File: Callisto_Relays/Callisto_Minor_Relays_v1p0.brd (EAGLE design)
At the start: 75 x 100 mm, 34 parts, among them J1 2-pos, J10 RJ45_TH_VERT, J2 RJ45_TH_VERT, J5 2-pos, J6 RJ45_TH_VERT, J7 2-pos, J8 RJ45_TH_VERT, J9 2-pos, U2 NPN, U3 NPN, U4 NPN, U5 NPN

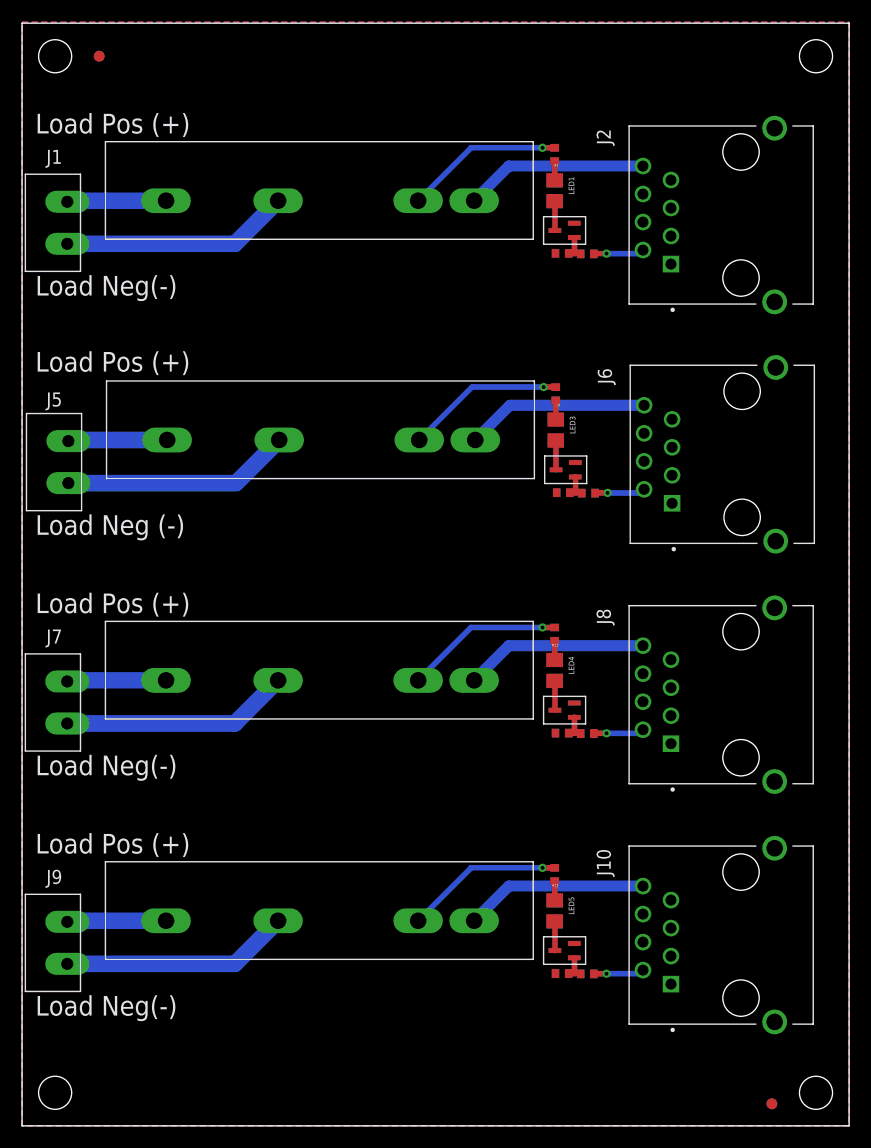
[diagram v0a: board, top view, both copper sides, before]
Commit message: Updated relay board.
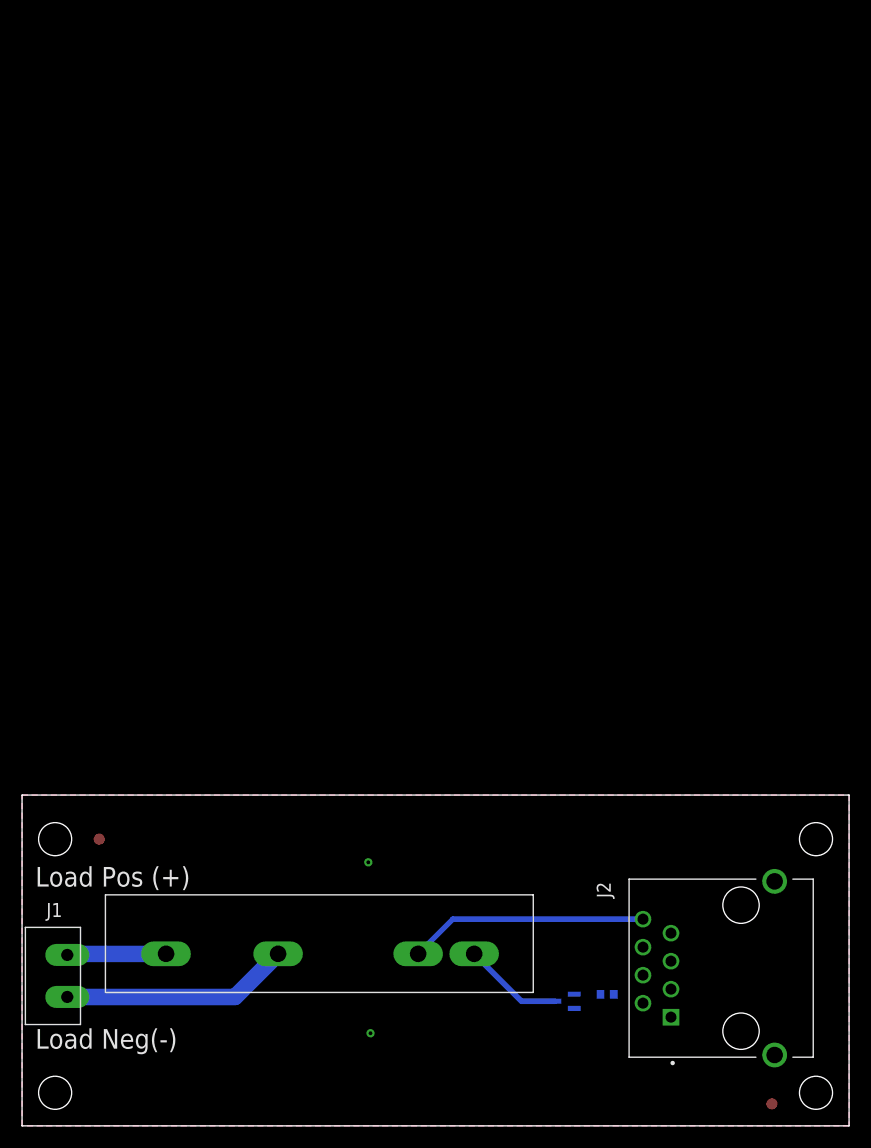
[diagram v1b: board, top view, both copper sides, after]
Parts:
- removed J10, J6, J8: RJ45_TH_VERT, 3D_MIG_Controller:ASSMANN_A-2014-2S-4-N-R
- removed J5, J7, J9: 2-pos, 3D_MIG_Controller:2_3.81MM_PITCH
- removed LED1, LED3, LED4, LED5: Green, 3D_MIG_Controller:0805
- removed R10, R13, R7: 1K, 3D_MIG_Controller:0402
- removed R11, R14, R2, R8: 10K, 3D_MIG_Controller:0402
- removed R12, R15, R3, R9: 470R0, 3D_MIG_Controller:0402
- removed U$5, U$6, U$7: RELAY_KYOTO_KF0604D, 3D_MIG_Controller:RELAY_KYOTO_KF0604D
- removed U3, U4, U5: NPN, 3D_MIG_Controller:SOT323
- R1: value 1K -> 500R0
- moved U$1 71.0 mm to (7.00, 26.0)
- moved U2 69.9 mm to (49.2, 11.3), flipped to the bottom, turned to 270 degrees
- moved U$3 68.3 mm to (41.0, 15.6)
- moved J1 68.3 mm to (4.10, 15.5)
- moved J2 68.3 mm to (65.2, 14.3)
- moved R1 67.2 mm to (53.1, 11.9), flipped to the bottom, turned to 90 degrees
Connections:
- removed net N$1: LED1.1, R3.P$1
- removed net N$10: LED4.1, R12.P$1
- removed net N$11: LED4.2, U4.3
- removed net N$12: R12.P$2, U$6.P$2
- removed net N$13: R7.P$2, R8.P$1, U3.1
- removed net N$14: LED3.1, R9.P$1
- removed net N$15: LED3.2, U3.3
- removed net N$16: R9.P$2, U$5.P$2
- removed net N$17: R13.P$2, R14.P$1, U5.1
- removed net N$18: LED5.1, R15.P$1
- removed net N$19: LED5.2, U5.3
- removed net N$20: R15.P$2, U$7.P$2
- removed net N$4: LED1.2, U2.3
- removed net N$9: R10.P$2, R11.P$1, U4.1
- removed net RELAY_2: J6.2, R7.P$1
- removed net RELAY_3: J8.2, R10.P$1
- removed net RELAY_4: J10.2, R13.P$1
- removed net RO_NEG_2: J5.P$2, U$5.P$3
- removed net RO_NEG_3: J7.P$2, U$6.P$3
- removed net RO_NEG_4: J9.P$2, U$7.P$3
- removed net RO_POS_2: J5.P$1, U$5.P$4
- removed net RO_POS_3: J7.P$1, U$6.P$4
- removed net RO_POS_4: J9.P$1, U$7.P$4
- new net NC: J2.4
- net GND: no longer J10.1, J10.4, J10.6, J2.4, J6.1, J6.4, J6.6, J8.1, J8.4, J8.6, R11.P$2, R14.P$2, R2.P$2, R8.P$2, U3.2, U4.2, U5.2
- net N$2: no longer R2.P$1
- net N$3: now also U$3.P$1, U2.3; no longer R3.P$2, U$3.P$2
- net VDD: no longer J10.5, J6.5, J8.5
- net VDD-12: no longer J10.7, J6.7, J8.7
- net VDD12: no longer J10.3, J6.3, J8.3
- net VDD5: now also U$3.P$2; no longer J10.8, J6.8, J8.8, U$3.P$1, U$5.P$1, U$6.P$1, U$7.P$1
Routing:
- net VDD5: track 66.5 -> 21.7 mm
- net RO_NEG_4: track 20.7 -> 0.00 mm
- net RO_NEG_2: track 20.7 -> 0.00 mm
- net RO_NEG_3: track 20.7 -> 0.00 mm
- net N$12: track 14.4 -> 0.00 mm, vias 1 -> 0
- net N$20: track 14.4 -> 0.00 mm, vias 1 -> 0
- net N$16: track 14.4 -> 0.00 mm, vias 1 -> 0
- net RO_POS_4: track 9.00 -> 0.00 mm
- net RO_POS_3: track 9.00 -> 0.00 mm
- net RO_POS_2: track 9.00 -> 0.00 mm
- net N$3: track 14.4 -> 9.10 mm, vias 1 -> 0
- net RELAY_4: track 4.59 -> 0.00 mm, vias 1 -> 0
- net RELAY_3: track 4.59 -> 0.00 mm, vias 1 -> 0
- net RELAY_1: track 4.59 -> 0.00 mm, vias 1 -> 0
- net RELAY_2: track 4.59 -> 0.00 mm, vias 1 -> 0
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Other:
- board size 75 x 100 mm -> 75 x 30 mm
- board text removed: "Load Neg (-)"
